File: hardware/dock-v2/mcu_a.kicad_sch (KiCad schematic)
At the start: 29 parts, among them SW301 SW_Push, SW302 SW_Push, U301 RP2354A, Y301 12MHz

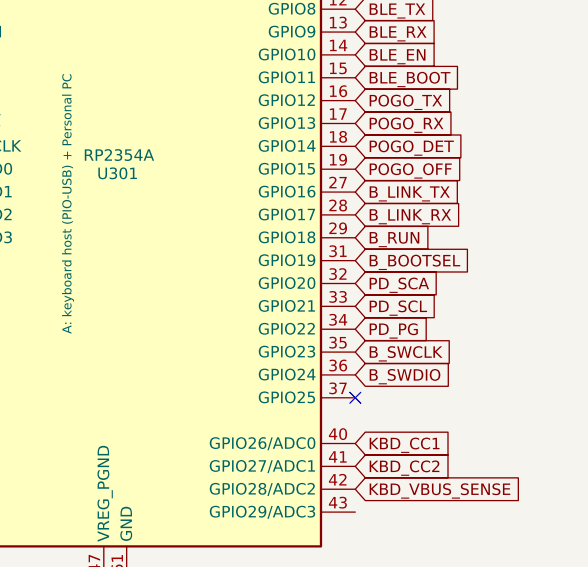
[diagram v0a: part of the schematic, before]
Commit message: Dock v2 schematic fixes after review (J601 7-pin, Q602/R609, part data)
KiCad had the sheets open when the 7-pin pogo and the pull-up/veto parts were
added, and its save restored the old state. Restored now (KiCad closed):
- J601 -> Conn_01x07, footprint dock:Pogo-7; R606 4.7k (1.45 A)
- Q602 + R609 (POGO_OFF veto) added back to the pogo sheet
- L101 footprint L_TechFuse_SL0630 / LCSC C207841 again
- R406/R407 had the 1k LCSC number (copied from R405): now C25744; notes fixed
  on R406, R407, R504
- references back to the docs: C205->C107, R223->R106, R306->R201, R304->R202;
  R103/R104 swapped so R103 is on SCL and R104 on SDA (they were swapped, harmless)
- global label typo PD_SCA -> PD_SDA (both ends)
- net classes: 3V3_PWR, 5V_PWR (Power) and *USB_DP/*USB_DN/*USB_DM (USB),
  matching the labels used in the schematic

check_wiring.py: accepts interchangeable pins (R/C/button/crystal either way
round, TPD4E1U06 channels in any order), warns on a reversed L301/L401,
reports missing parts.

Co-Authored-By: Claude Opus 5.5 <noreply@anthropic.com>
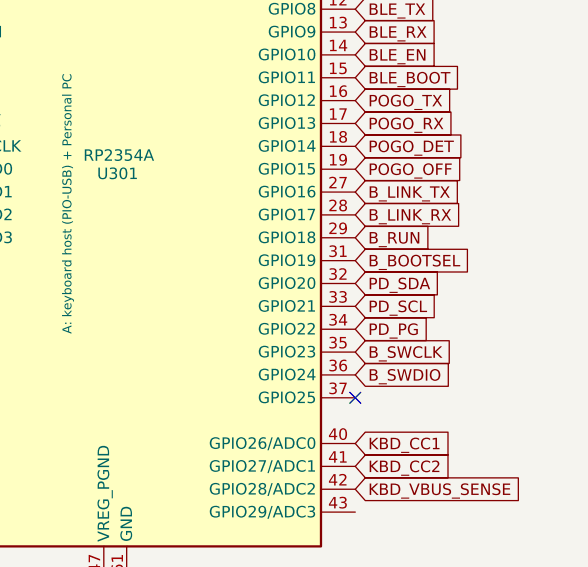
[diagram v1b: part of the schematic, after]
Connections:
- net PD_SCA renamed PD_SDA
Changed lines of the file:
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@@
 		)
 	)
-	(global_label "PD_SCA"
+	(global_label "PD_SDA"
 		(shape input)
 		(at 209.55 132.08 0)
